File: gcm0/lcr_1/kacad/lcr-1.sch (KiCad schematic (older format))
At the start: 84 parts, among them J1 +9, J11 SWD, J2 Conn_01x02_Male, J3 Conn_01x02_Male, J6 GND, Q1 BC547, Q2 BC547, SW1 SW_Push, SW2 SW_Push, U1 NE5532, U2 LM2596S-5, U3 LM7805_TO220, U4 CD4053B, U5 STM32F030F4P6, U6 LM1117-3.3, U7 CD4052B, U8 TL084, U9 74HC595, Y1 8M

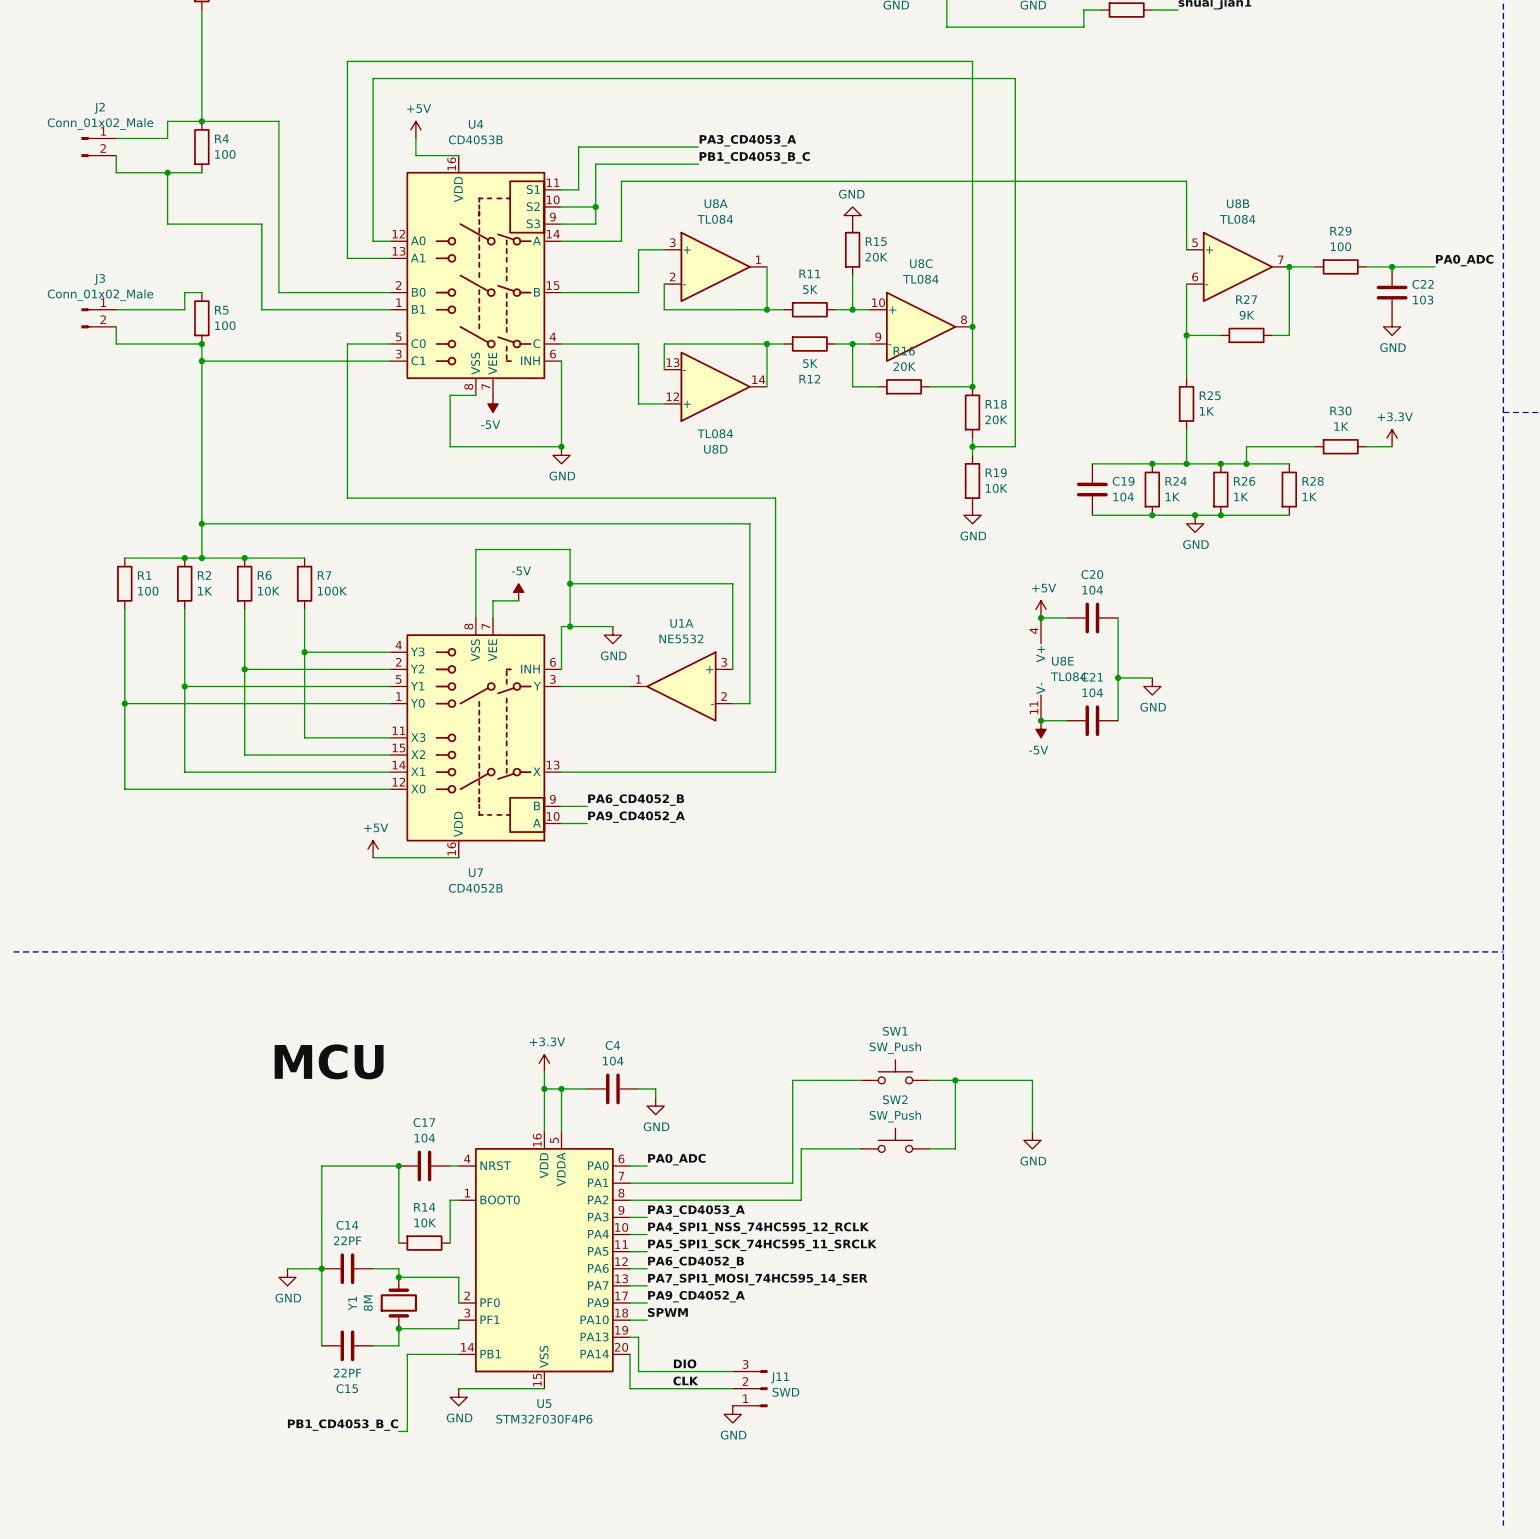
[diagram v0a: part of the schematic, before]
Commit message: 电路偏置改错
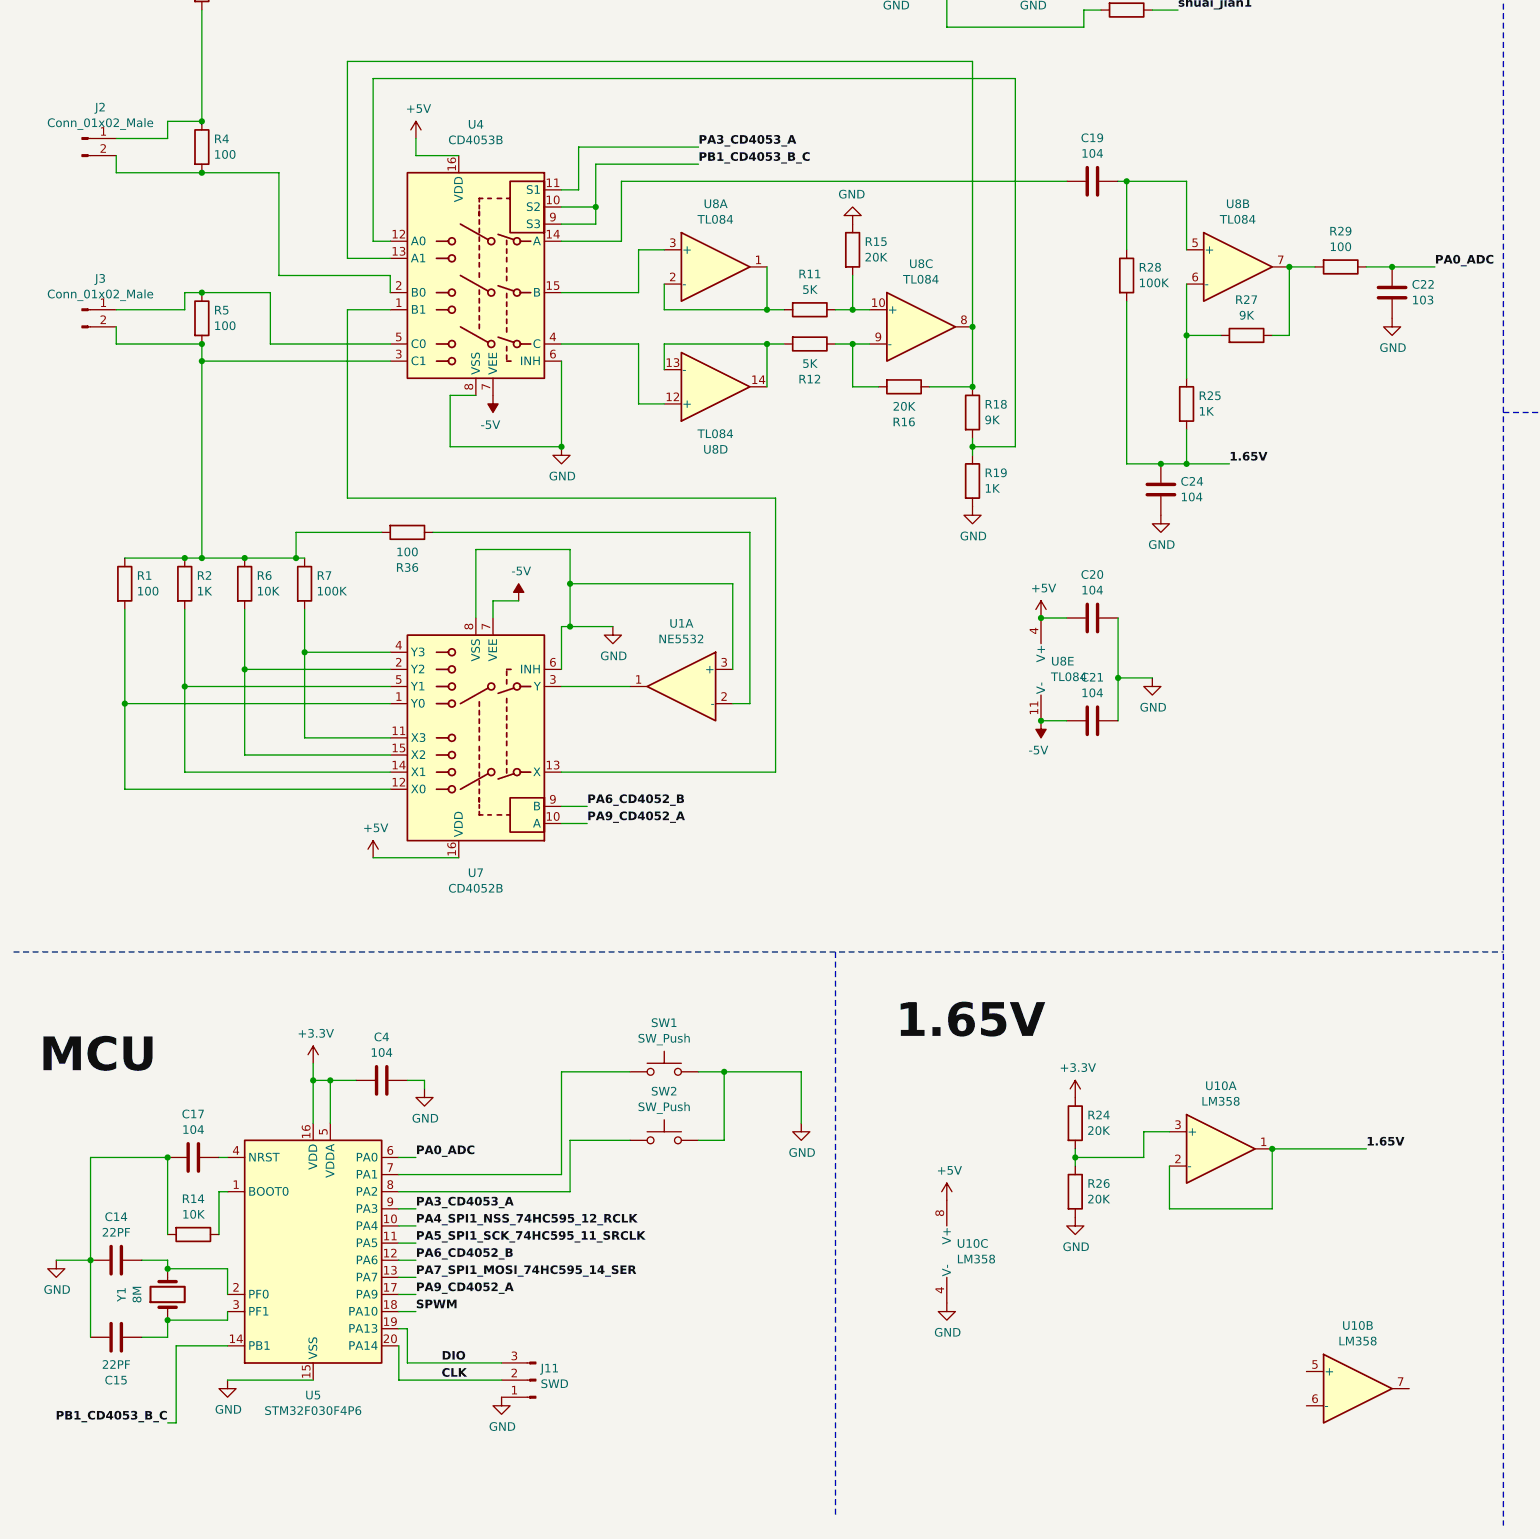
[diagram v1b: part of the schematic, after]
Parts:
- removed R30: 1K, symbol Device:R
- added C24: 104, symbol Device:C
- added R36: 100, symbol Device:R
- added U10: LM358, symbol Amplifier_Operational:LM358
- R18: value 20K -> 9K
- R19: value 10K -> 1K
- R24, R26: value 1K -> 20K
- R28: value 1K -> 100K
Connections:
- net +3V3: now also R24.1
- net +5V: now also U10.8 (V+)
- net GND: now also C24.2, U10.4 (V-); no longer C19.2, R24.2, R28.2
- net at J3.2 (Pin_2), R1.1, R2.1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: now also R36.2; no longer U1.2 (-)
- net at J2.1 (Pin_1), R3.2, R4.1: no longer U4.2 (B0)
- net at J2.2 (Pin_2), R4.2: now also U4.2 (B0); no longer U4.1 (B1)
- net at J3.1 (Pin_1), R5.1: now also U4.5 (C0)
- net at U7.13 (X): now also U4.1 (B1); no longer U4.5 (C0)
- net at U8.5 (+): now also C19.1, R28.1; no longer U4.14 (A)
- new net: R24.2, R26.1, U10.3 (+)
- new net: C19.2, U4.14 (A)
- new net: R36.1, U1.2 (-)
- new net 1.65V: C24.1, R25.2, R28.2, U10.1, U10.2 (-)
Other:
- moved on the sheet: C14, C15, C17, C4, J11, R14, SW1, SW2, U5, Y1

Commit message: 修改小数点位置
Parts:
- removed BT1: 9V, symbol Device:Battery_Cell
- removed D1: 1N4007, Diode_THT:D_DO-41_SOD81_P10.16mm_Horizontal, symbol Diode:1N4007
- removed D2: 1N5822, Diode_THT:D_DO-201AD_P15.24mm_Horizontal, symbol Diode:1N5822
- removed J2, J3: Conn_01x02_Male, symbol Connector:Conn_01x02_Male
- removed R10, R17, R21: 1K, symbol Device:R
- removed R20: 200, symbol Device:R
- added C12, C13, C19, C8: 104, Capacitor_THT:C_Disc_D3.0mm_W2.0mm_P2.50mm, symbol Device:C
- added D2: 1N5819, Diode_SMD:D_SMA_Handsoldering, symbol Diode:1N5819
- added J10, J23, J34, J7, J8: 5V, Connector_Pin:Pin_D0.7mm_L6.5mm_W1.8mm_FlatFork, symbol Connector:Conn_01x01_Male
- added J12, J22, J33: -5V, Connector_Pin:Pin_D0.7mm_L6.5mm_W1.8mm_FlatFork, symbol Connector:Conn_01x01_Male
- added J14, J17: PA3, Connector_Pin:Pin_D0.7mm_L6.5mm_W1.8mm_FlatFork, symbol Connector:Conn_01x01_Male
- added J15, J25: SPWM, Connector_Pin:Pin_D0.7mm_L6.5mm_W1.8mm_FlatFork, symbol Connector:Conn_01x01_Male
- added J16, J18: PA9, Connector_Pin:Pin_D0.7mm_L6.5mm_W1.8mm_FlatFork, symbol Connector:Conn_01x01_Male
- added J19, J20: PA6, Connector_Pin:Pin_D0.7mm_L6.5mm_W1.8mm_FlatFork, symbol Connector:Conn_01x01_Male
- added J2: Hc, Connector_Pin:Pin_D1.3mm_L11.0mm_LooseFit, symbol Connector:Conn_01x01_Male
- added J21: PB1, Connector_Pin:Pin_D0.7mm_L6.5mm_W1.8mm_FlatFork, symbol Connector:Conn_01x01_Male
- added J24: 3.3, Connector_Pin:Pin_D0.7mm_L6.5mm_W1.8mm_FlatFork, symbol Connector:Conn_01x01_Male
- added J26, J27: 1.65V, Connector_Pin:Pin_D0.7mm_L6.5mm_W1.8mm_FlatFork, symbol Connector:Conn_01x01_Male
- added J28, J36: shuai_jian1, Connector_Pin:Pin_D0.7mm_L6.5mm_W1.8mm_FlatFork, symbol Connector:Conn_01x01_Male
- added J29, J37: shuan_jian, Connector_Pin:Pin_D0.7mm_L6.5mm_W1.8mm_FlatFork, symbol Connector:Conn_01x01_Male
- added J3: Hp, Connector_Pin:Pin_D1.3mm_L11.0mm_LooseFit, symbol Connector:Conn_01x01_Male
- added J30, J9: ADC, Connector_Pin:Pin_D0.7mm_L6.5mm_W1.8mm_FlatFork, symbol Connector:Conn_01x01_Male
- added J31: +9V, Connector_Pin:Pin_D1.3mm_L11.0mm_LooseFit, symbol Connector:Conn_01x01_Male
- added J32: GND, Connector_Pin:Pin_D1.3mm_L11.0mm_LooseFit, symbol Connector:Conn_01x01_Male
- added J35, J38: 3.3V, Connector_Pin:Pin_D0.7mm_L6.5mm_W1.8mm_FlatFork, symbol Connector:Conn_01x01_Male
- added J4: Lp, Connector_Pin:Pin_D1.3mm_L11.0mm_LooseFit, symbol Connector:Conn_01x01_Male
- added J5: Lc, Connector_Pin:Pin_D1.3mm_L11.0mm_LooseFit, symbol Connector:Conn_01x01_Male
- added Q2: BC547, Package_TO_SOT_THT:TO-92_Inline_Wide, symbol Transistor_BJT:BC547
- added R16, R25: 1K, Resistor_THT:R_Axial_DIN0204_L3.6mm_D1.6mm_P2.54mm_Vertical, symbol Device:R
- C10: renamed from C16; footprint (none) -> Capacitor_THT:C_Disc_D3.0mm_W2.0mm_P2.50mm
- C11: renamed from C8; footprint (none) -> Capacitor_THT:C_Disc_D3.0mm_W2.0mm_P2.50mm
- C14: renamed from C9; footprint (none) -> Capacitor_THT:C_Disc_D3.0mm_W2.0mm_P2.50mm
- C15: renamed from C19; footprint (none) -> Capacitor_THT:C_Disc_D3.0mm_W2.0mm_P2.50mm
- C16: renamed from C20; footprint (none) -> Capacitor_THT:C_Disc_D3.0mm_W2.0mm_P2.50mm
- C17: renamed from C21; footprint (none) -> Capacitor_THT:C_Disc_D3.0mm_W2.0mm_P2.50mm
- C18: renamed from C24; footprint (none) -> Capacitor_THT:C_Disc_D3.0mm_W2.0mm_P2.50mm
- C20: renamed from C22; footprint (none) -> Capacitor_THT:C_Disc_D3.0mm_W2.0mm_P2.50mm
- C25: renamed from C23; footprint (none) -> Capacitor_THT:C_Disc_D3.0mm_W2.0mm_P2.50mm
- C28: renamed from C18; value 105 -> 106
- C3: renamed from C1; footprint (none) -> Capacitor_THT:C_Disc_D3.0mm_W2.0mm_P2.50mm
- C4: renamed from C2; footprint (none) -> Capacitor_THT:C_Disc_D3.0mm_W2.0mm_P2.50mm
- C6: renamed from C4; footprint (none) -> Capacitor_THT:C_Disc_D3.0mm_W2.0mm_P2.50mm
- C7: renamed from C3; footprint (none) -> Capacitor_THT:C_Disc_D3.0mm_W2.0mm_P2.50mm
- C9: renamed from C5; footprint (none) -> Capacitor_THT:C_Disc_D3.0mm_W2.0mm_P2.50mm
- DS1: footprint Connector_PinHeader_2.54mm:PinHeader_1x16_P2.54mm_Vertical -> Display:WC1602A
- J1: value +9 -> -5V; footprint Connector_PinHeader_2.54mm:PinHeader_1x01_P2.54mm_Vertical -> Connector_Pin:Pin_D0.7mm_L6.5mm_W1.8mm_FlatFork
- J6: value GND -> PB1; footprint Connector_PinHeader_2.54mm:PinHeader_1x01_P2.54mm_Vertical -> Connector_Pin:Pin_D0.7mm_L6.5mm_W1.8mm_FlatFork
- Q1: footprint Package_TO_SOT_THT:TO-92_Inline -> Package_TO_SOT_THT:TO-92_Inline_Wide
- Q3: renamed from Q2; footprint Package_TO_SOT_THT:TO-92_Inline -> Package_TO_SOT_THT:TO-92_Inline_Wide
- R1, R12, R2, R27: footprint (none) -> Resistor_THT:R_Axial_DIN0204_L3.6mm_D1.6mm_P2.54mm_Vertical
- R10: renamed from R8; footprint (none) -> Resistor_THT:R_Axial_DIN0204_L3.6mm_D1.6mm_P2.54mm_Vertical
- R11: renamed from R9; footprint (none) -> Resistor_THT:R_Axial_DIN0204_L3.6mm_D1.6mm_P2.54mm_Vertical
- R13: renamed from R11; footprint (none) -> Resistor_THT:R_Axial_DIN0204_L3.6mm_D1.6mm_P2.54mm_Vertical
- R14: renamed from R15; footprint (none) -> Resistor_THT:R_Axial_DIN0204_L3.6mm_D1.6mm_P2.54mm_Vertical
- R15: renamed from R16; footprint (none) -> Resistor_THT:R_Axial_DIN0204_L3.6mm_D1.6mm_P2.54mm_Vertical
- R17: renamed from R18; footprint (none) -> Resistor_THT:R_Axial_DIN0204_L3.6mm_D1.6mm_P2.54mm_Vertical
- R18: renamed from R19; footprint (none) -> Resistor_THT:R_Axial_DIN0204_L3.6mm_D1.6mm_P2.54mm_Vertical
- R19: renamed from R13; footprint (none) -> Resistor_THT:R_Axial_DIN0204_L3.6mm_D1.6mm_P2.54mm_Vertical
- R20: renamed from R24; footprint (none) -> Resistor_THT:R_Axial_DIN0204_L3.6mm_D1.6mm_P2.54mm_Vertical
- R21: renamed from R26; footprint (none) -> Resistor_THT:R_Axial_DIN0204_L3.6mm_D1.6mm_P2.54mm_Vertical
- R22: renamed from R28; footprint (none) -> Resistor_THT:R_Axial_DIN0204_L3.6mm_D1.6mm_P2.54mm_Vertical
- R23: renamed from R22; footprint (none) -> Resistor_THT:R_Axial_DIN0204_L3.6mm_D1.6mm_P2.54mm_Vertical
- R24: renamed from R23; footprint (none) -> Resistor_THT:R_Axial_DIN0204_L3.6mm_D1.6mm_P2.54mm_Vertical
- R26: renamed from R25; footprint (none) -> Resistor_THT:R_Axial_DIN0204_L3.6mm_D1.6mm_P2.54mm_Vertical
- R28: renamed from R29; footprint (none) -> Resistor_THT:R_Axial_DIN0204_L3.6mm_D1.6mm_P2.54mm_Vertical
- R29: renamed from R31; footprint (none) -> Resistor_THT:R_Axial_DIN0204_L3.6mm_D1.6mm_P2.54mm_Vertical
- R3: renamed from R14; footprint Resistor_THT:R_Axial_DIN0207_L6.3mm_D2.5mm_P5.08mm_Vertical -> Resistor_THT:R_Axial_DIN0204_L3.6mm_D1.6mm_P2.54mm_Vertical
- R30: renamed from R32; footprint (none) -> Resistor_THT:R_Axial_DIN0204_L3.6mm_D1.6mm_P2.54mm_Vertical
- R31: renamed from R33; footprint (none) -> Resistor_THT:R_Axial_DIN0204_L3.6mm_D1.6mm_P2.54mm_Vertical
- R32: renamed from R34; footprint (none) -> Resistor_THT:R_Axial_DIN0204_L3.6mm_D1.6mm_P2.54mm_Vertical
- R33: renamed from R35; footprint (none) -> Resistor_THT:R_Axial_DIN0204_L3.6mm_D1.6mm_P2.54mm_Vertical
- R4: renamed from R3; footprint (none) -> Resistor_THT:R_Axial_DIN0204_L3.6mm_D1.6mm_P2.54mm_Vertical
- R5: renamed from R4; footprint (none) -> Resistor_THT:R_Axial_DIN0204_L3.6mm_D1.6mm_P2.54mm_Vertical
- R6: renamed from R5; footprint (none) -> Resistor_THT:R_Axial_DIN0204_L3.6mm_D1.6mm_P2.54mm_Vertical
- R7: renamed from R6; footprint (none) -> Resistor_THT:R_Axial_DIN0204_L3.6mm_D1.6mm_P2.54mm_Vertical
- R8: renamed from R7; footprint (none) -> Resistor_THT:R_Axial_DIN0204_L3.6mm_D1.6mm_P2.54mm_Vertical
- R9: renamed from R36; footprint (none) -> Resistor_THT:R_Axial_DIN0204_L3.6mm_D1.6mm_P2.54mm_Vertical
- SW1, SW2: footprint (none) -> Button_Switch_THT:SW_PUSH_6mm_H7.3mm
- U1: footprint (none) -> Package_DIP:DIP-8_W7.62mm
- U3: renamed from U4; footprint (none) -> Package_DIP:DIP-16_W7.62mm
- U4: renamed from U7; footprint (none) -> Package_DIP:DIP-16_W7.62mm
- U5: renamed from U8; footprint (none) -> Package_DIP:DIP-14_W7.62mm
- U6: renamed from U10; footprint (none) -> Package_DIP:DIP-8_W7.62mm
- U8: renamed from U3; footprint Package_TO_SOT_THT:TO-220-3_Vertical -> Package_TO_SOT_THT:TO-220-3_Horizontal_TabDown
- renumbered C14 to C1, C15 to C2, C6 to C21, C7 to C22, C10 to C23, C11 to C24, C12 to C26, C13 to C27, C17 to C5, D3 to D1, D8 to D3, U2 to U10, U5 to U2, U9 to U7, U6 to U9
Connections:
- net +3V3: now also U6.8 (V+), J24.1 (Pin_1), J35.1 (Pin_1), J38.1 (Pin_1)
- net +5V: now also U9.3 (VI), J10.1 (Pin_1), J23.1 (Pin_1), J34.1 (Pin_1), J7.1 (Pin_1), J8.1 (Pin_1); no longer U6.8 (V+)
- net +9V: now also J31.1 (Pin_1); no longer J1.1 (Pin_1)
- net -5V: now also J1.1 (Pin_1), D2.2 (A), J12.1 (Pin_1), J22.1 (Pin_1), J33.1 (Pin_1)
- net 1.65V: now also C19.1, J26.1 (Pin_1), J27.1 (Pin_1)
- net GND: now also Q3.3 (E), C13.2, C19.2, J32.1 (Pin_1), Q2.3 (E); no longer J6.1 (Pin_1), Q3.1 (C)
- net PA0_ADC: now also J30.1 (Pin_1), J9.1 (Pin_1)
- net PA3_CD4053_A: now also J14.1 (Pin_1), J17.1 (Pin_1)
- net PA6_CD4052_B: now also J19.1 (Pin_1), J20.1 (Pin_1)
- net PA9_CD4052_A: now also J16.1 (Pin_1), J18.1 (Pin_1)
- net PB1_CD4053_B_C: now also J6.1 (Pin_1), J21.1 (Pin_1)
- net SPWM: now also R19.1, J15.1 (Pin_1), J25.1 (Pin_1)
- net shai_jian: now also J29.1 (Pin_1), J37.1 (Pin_1)
- net shuai_jian1: now also J28.1 (Pin_1), J36.1 (Pin_1), R25.1
- net at L1.2, U10.2 (OUT): now also D2.1 (K)
- net at R20.2, R21.1, U6.3 (+): now also C13.1
- net at U6.6 (-): now also U6.7
- net Hc: now reaches R4.2, R5.1
- net Hc: now also J2.1 (Pin_1)
- net Hp: now reaches R5.2, U3.2 (B0)
- net Hp: now also J3.1 (Pin_1)
- net Lp: now reaches R6.1, U3.5 (C0)
- net Lp: now also J4.1 (Pin_1)
- net Lc: now reaches R1.1, R2.1, R6.2, R7.1, R8.1, R9.2, U3.3 (C1)
- net Lc: now also J5.1 (Pin_1)
- net at U5.1, U5.2 (-): now also R12.2; no longer R13.2
- net at R14.2, U5.10 (+): now also R12.1; no longer R13.1
- net at R15.2, U5.9 (-): now also R13.1; no longer R12.1
- net at U5.13 (-), U5.14: now also R13.2; no longer R12.2
- net at C7.1, C9.1, R11.2: now also C8.1
- net at C11.1, R11.1: now also C10.1, R16.2
- net at C14.1, R19.2: now also C12.1, R16.1
- net at C10.2: now also Q2.1 (C); no longer Q1.1 (C)
- net at R24.2: now also Q2.2 (B); no longer Q1.2 (B)
- new net: C8.2, Q1.1 (C)
- new net: Q1.2 (B), R25.2
- new net: C12.2, Q3.1 (C)
- no-connect marks 5 -> 6
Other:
- note added: "D\nU\nT\n"
- moved on the sheet: C10, C11, C14, C20, C7, C9, Q1, Q3, R10, R11, R12, R13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

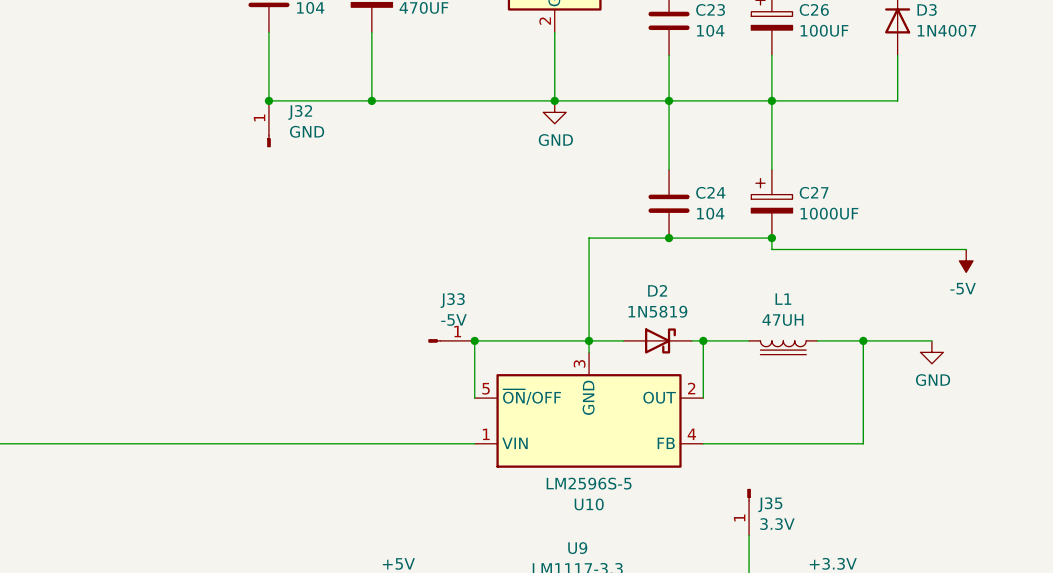
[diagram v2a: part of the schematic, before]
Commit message: LM2596延迟电路
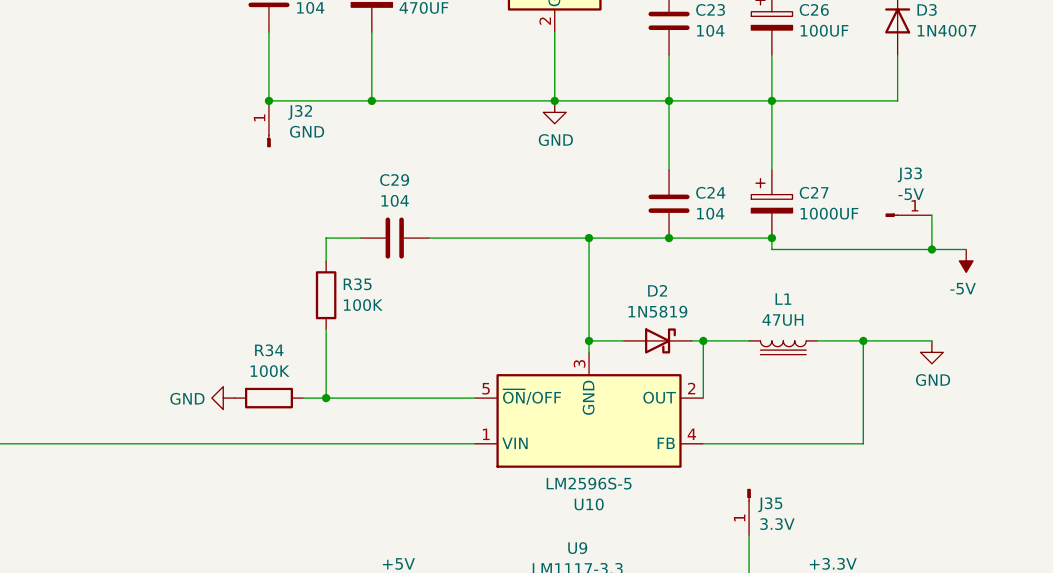
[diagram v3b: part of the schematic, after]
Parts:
- added C29: 104, symbol Device:C
- added R34, R35: 100K, symbol Device:R
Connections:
- net -5V: now also C29.1; no longer U10.5 (~ON~/OFF)
- net GND: now also R34.2
- new net: R34.1, R35.2, U10.5 (~ON~/OFF)
- new net: C29.2, R35.1
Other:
- moved on the sheet: J33
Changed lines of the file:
@@
 Wire Wire Line
 	14900 7150 14900 7100
-Wire Wire Line
-	15750 7150 14900 7150
 $Comp
 L power:-5V #PWR054
@@
 	0    1    1    0
 $EndComp
-Wire Wire Line
-	14100 7550 13600 7550
 Connection ~ 14100 7550
 Wire Wire Line
 	14100 7600 14100 7550
-Wire Wire Line
-	13600 7550 13600 7800
 Wire Wire Line
 	14250 7550 14100 7550
@@
 L Connector:Conn_01x01_Male J33
 U 1 1 61B9A1FB
-P 13400 7550
-F 0 "J33" H 13508 7731 50  0000 C CNN
-F 1 "-5V" H 13508 7640 50  0000 C CNN
-F 2 "Connector_Pin:Pin_D0.7mm_L6.5mm_W1.8mm_FlatFork" H 13400 7550 50  0001 C CNN
-F 3 "~" H 13400 7550 50  0001 C CNN
-	1    13400 7550
-	1    0    0    -1
-$EndComp
-Connection ~ 13600 7550
+P 15400 7000
+F 0 "J33" H 15508 7181 50  0000 C CNN
+F 1 "-5V" H 15508 7090 50  0000 C CNN
+F 2 "Connector_Pin:Pin_D0.7mm_L6.5mm_W1.8mm_FlatFork" H 15400 7000 50  0001 C CNN
+F 3 "~" H 15400 7000 50  0001 C CNN
+	1    15400 7000
+	1    0    0    -1
+$EndComp
 $Comp
 L Connector:Conn_01x01_Male J35
@@
 Wire Wire Line
 	3250 5900 3250 6000
+$Comp
+L Device:C C29
+U 1 1 614229B0
+P 13250 7100
+F 0 "C29" V 12998 7100 50  0000 C CNN
+F 1 "104" V 13089 7100 50  0000 C CNN
+F 2 "" H 13288 6950 50  0001 C CNN
+F 3 "~" H 13250 7100 50  0001 C CNN
+	1    13250 7100
+	0    1    1    0
+$EndComp
+$Comp
+L Device:R R35
+U 1 1 61426DC8
+P 12950 7350
+F 0 "R35" H 13020 7396 50  0000 L CNN
+F 1 "100K" H 13020 7305 50  0000 L CNN
+F 2 "" V 12880 7350 50  0001 C CNN
+F 3 "~" H 12950 7350 50  0001 C CNN
+	1    12950 7350
+	1    0    0    -1
+$EndComp
+$Comp
+L Device:R R34
+U 1 1 61428E4F
+P 12700 7800
+F 0 "R34" V 12493 7800 50  0000 C CNN
+F 1 "100K" V 12584 7800 50  0000 C CNN
+F 2 "" V 12630 7800 50  0001 C CNN
+F 3 "~" H 12700 7800 50  0001 C CNN
+	1    12700 7800
+	0    1    1    0
+$EndComp
+Wire Wire Line
+	13400 7100 14100 7100
+Connection ~ 14100 7100
+Wire Wire Line
+	13100 7100 12950 7100
+Wire Wire Line
+	12950 7100 12950 7200
+Wire Wire Line
+	12950 7800 13600 7800
+Wire Wire Line
+	12950 7500 12950 7800
+Wire Wire Line
+	12850 7800 12950 7800
+Connection ~ 12950 7800
+$Comp
+L power:GND #PWR055
+U 1 1 6152BAF3
+P 12550 7800
+F 0 "#PWR055" H 12550 7550 50  0001 C CNN
+F 1 "GND" V 12555 7672 50  0000 R CNN
+F 2 "" H 12550 7800 50  0001 C CNN
+F 3 "" H 12550 7800 50  0001 C CNN
+	1    12550 7800
+	0    1    1    0
+$EndComp
+Wire Wire Line
+	15600 7000 15600 7150
+Wire Wire Line
+	14900 7150 15600 7150
+Connection ~ 15600 7150
+Wire Wire Line
+	15600 7150 15750 7150
 $EndSCHEMATC
